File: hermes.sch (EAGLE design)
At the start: 29 parts, among them IC1 MIC5219-3.3BML

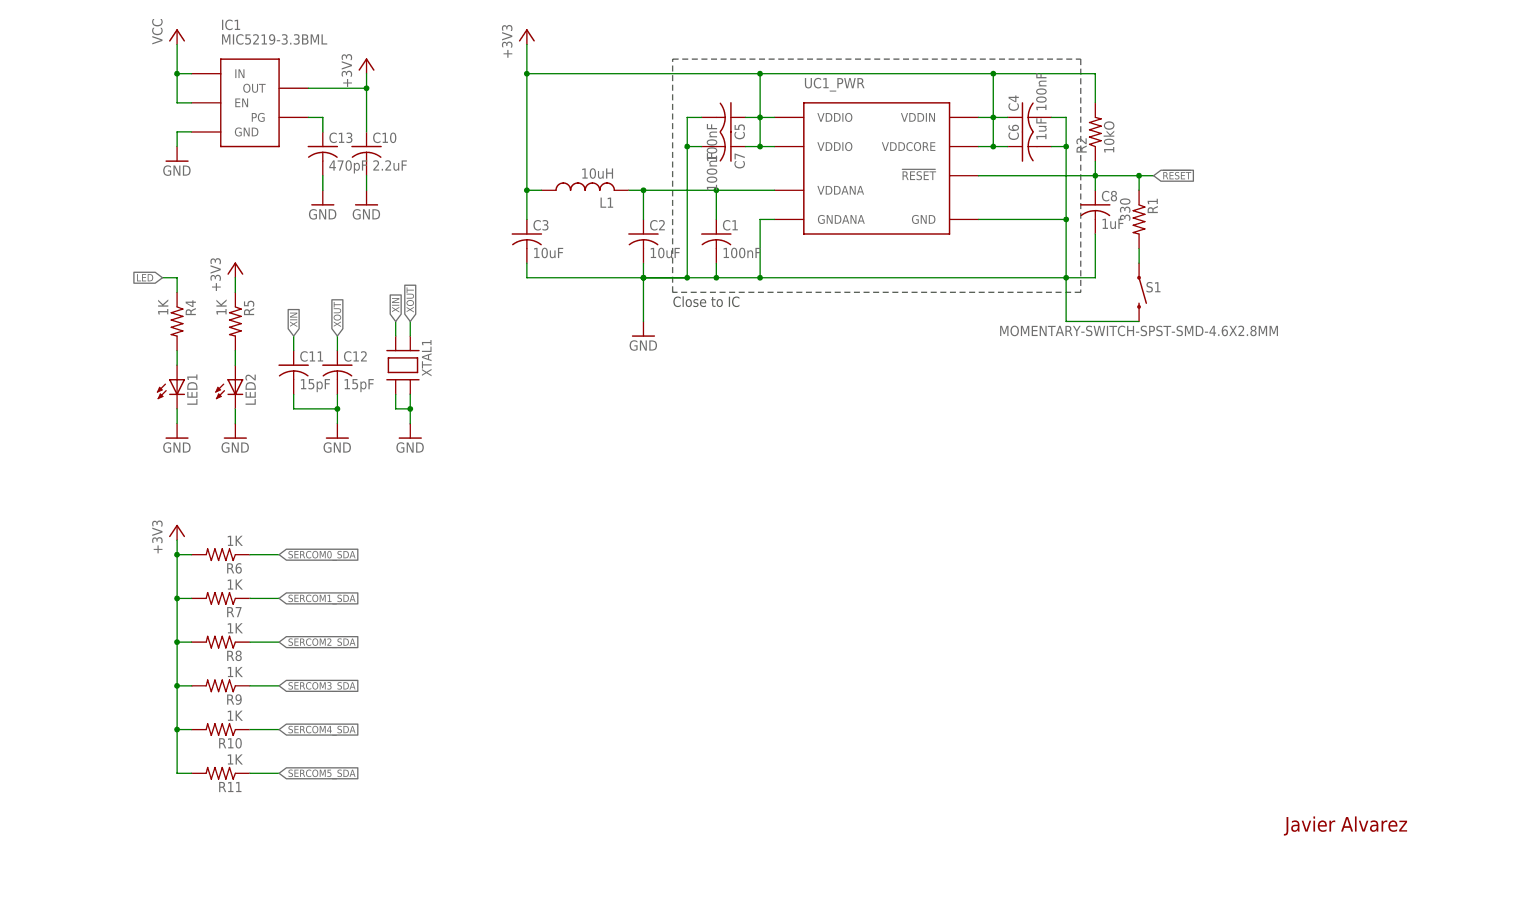
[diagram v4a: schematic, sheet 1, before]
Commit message: -Remove Reset switch -Add programming port -Correct minor connection issues
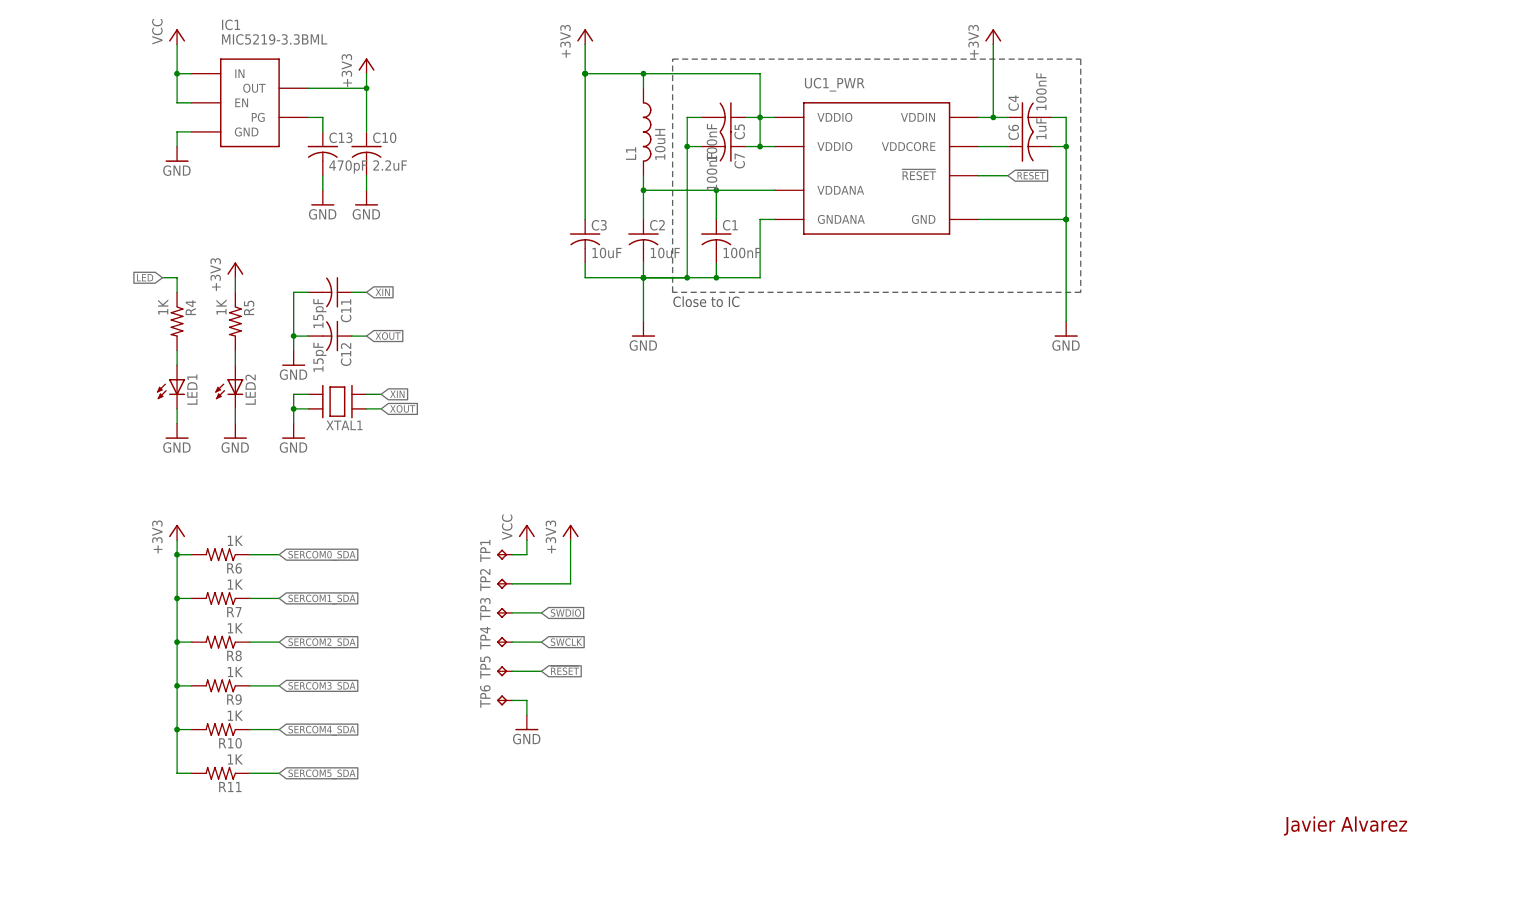
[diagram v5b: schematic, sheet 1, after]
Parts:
- removed C8: 1uF, rcl:C-USC0201
- removed R1: 330, rcl:R-US_R0201
- removed R2: 10kO, rcl:R-US_R0201
- removed S1: MOMENTARY-SWITCH-SPST-SMD-4.6X2.8MM, SparkFun-Switches:MOMENTARY-SWITCH-SPST-SMD-4.6X2.8MM
- added TP1, TP2, TP3, TP4, TP5, TP6: TPB2,54, testpad:TPB2,54
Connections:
- removed net N$5: R1.2, S1.1
- new net N$3: C6.1, UC1_PWR.VDDCORE
- net !RESET: now also TP5.TP; no longer C8.1, R1.1, R2.1
- net +3V3: now also TP2.TP; no longer C6.1, R2.2, UC1_PWR.VDDCORE
- net GND: now also TP6.TP; no longer C8.2, S1.2
- net SWCLK: now also TP4.TP
- net SWDIO: now also TP3.TP
- net VCC: now also TP1.TP
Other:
- moved on the sheet: C11, C12, C3, L1, XTAL1

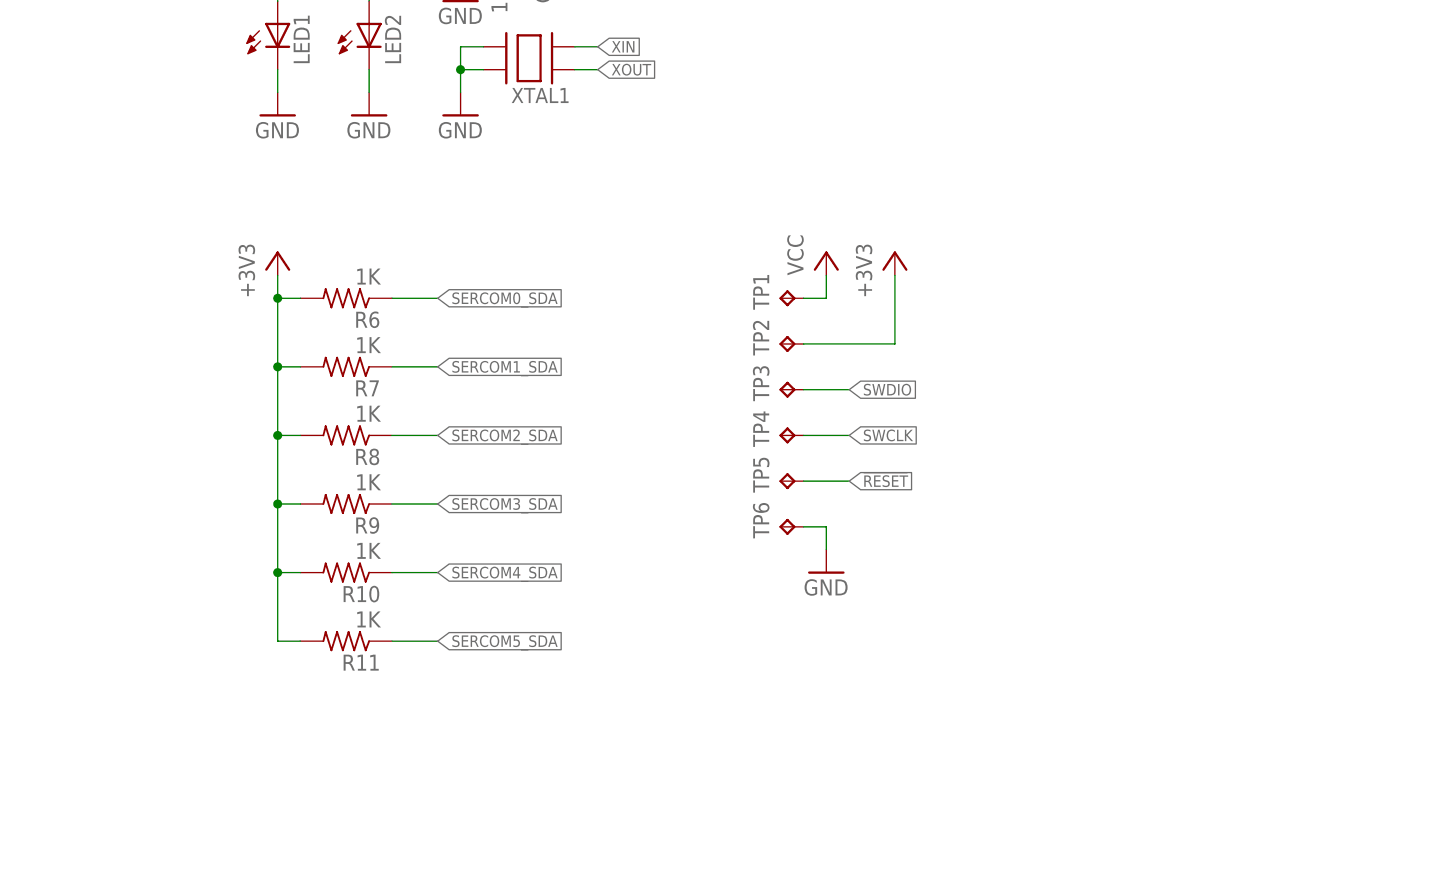
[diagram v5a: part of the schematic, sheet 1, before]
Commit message: -Correct README.md specifications -Add custom pads to library -Add programming connection to schematics
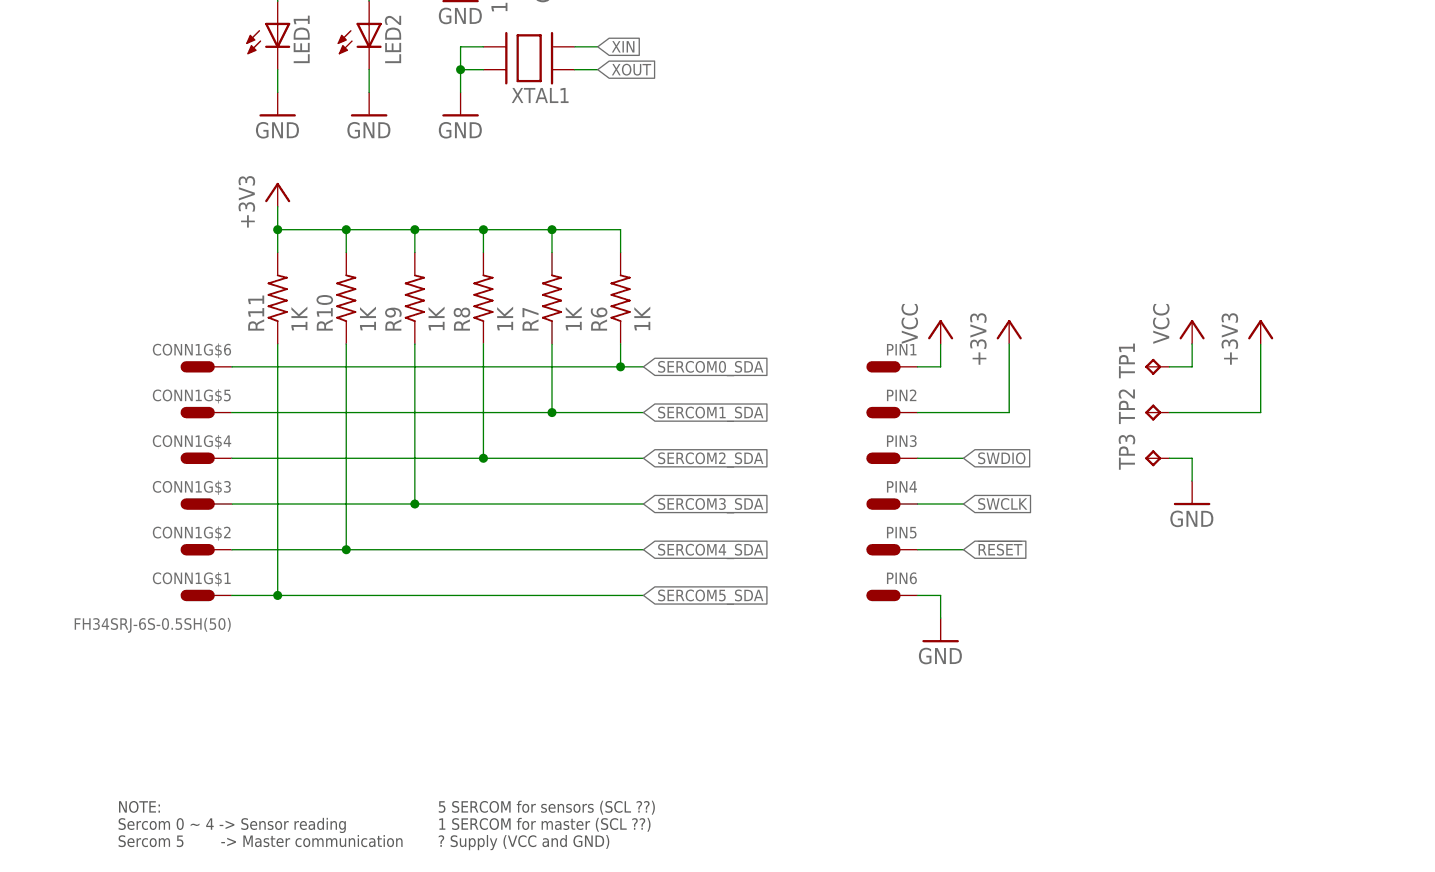
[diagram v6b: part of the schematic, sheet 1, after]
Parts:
- removed TP4, TP5, TP6: TPB2,54, testpad:TPB2,54
- added CONN1: FH34SRJ-6S-0.5SH(50), Hermes_lib:FH34SRJ-6S-0.5SH(50)
- added PIN1, PIN2, PIN3, PIN4, PIN5, PIN6: SINGLE-PIN, Hermes_lib:SINGLE-PIN
- TP1, TP2, TP3: value TPB2,54 -> TPB1,27; device testpad:TPB2,54 -> testpad:TPB1,27
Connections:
- net !RESET: now also PIN5.P$1; no longer TP5.TP
- net +3V3: now also PIN2.P$1
- net GND: now also PIN6.P$1, TP3.TP; no longer TP6.TP
- net SERCOM0_SDA: now also CONN1G$6.P$1
- net SERCOM1_SDA: now also CONN1G$5.P$1
- net SERCOM2_SDA: now also CONN1G$4.P$1
- net SERCOM3_SDA: now also CONN1G$3.P$1
- net SERCOM4_SDA: now also CONN1G$2.P$1
- net SERCOM5_SDA: now also CONN1G$1.P$1
- net SWCLK: now also PIN4.P$1; no longer TP4.TP
- net SWDIO: now also PIN3.P$1; no longer TP3.TP
- net VCC: now also PIN1.P$1
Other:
- note added: "5 SERCOM for sensors (SCL ??) 1 SERCOM for master (SCL ??) ? Supply (VCC and GND)"
- note added: "NOTE: Sercom 0 ~ 4 -> Sensor reading Sercom 5 -> Master communication"
- moved on the sheet: R10, R11, R6, R7, R8, R9, TP1, TP2, TP3

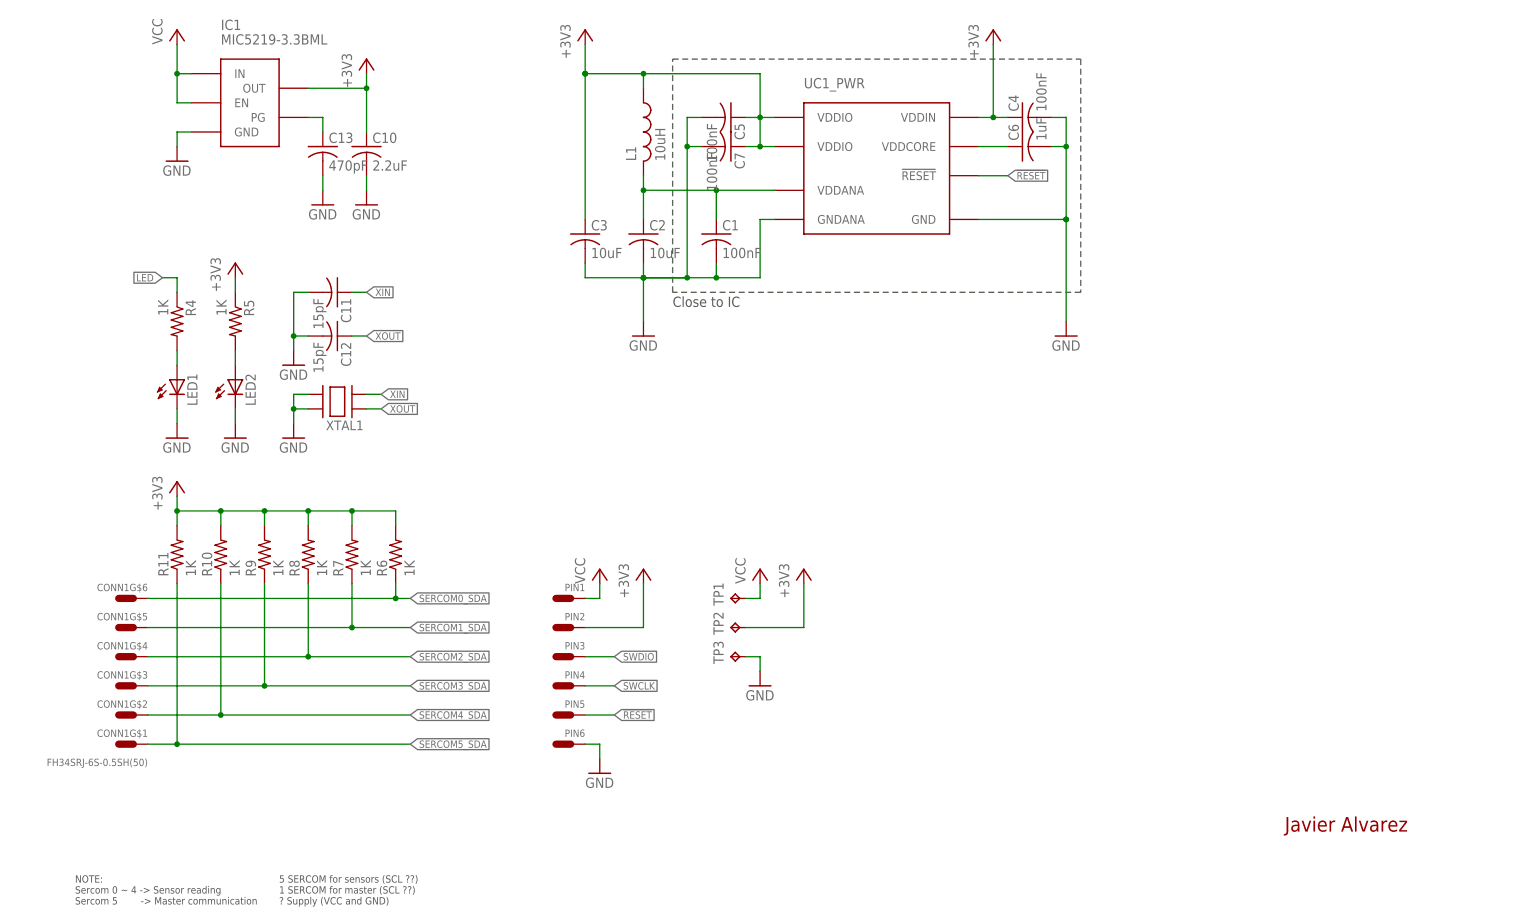
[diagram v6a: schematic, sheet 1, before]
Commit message: -Confirm cabling -Add information
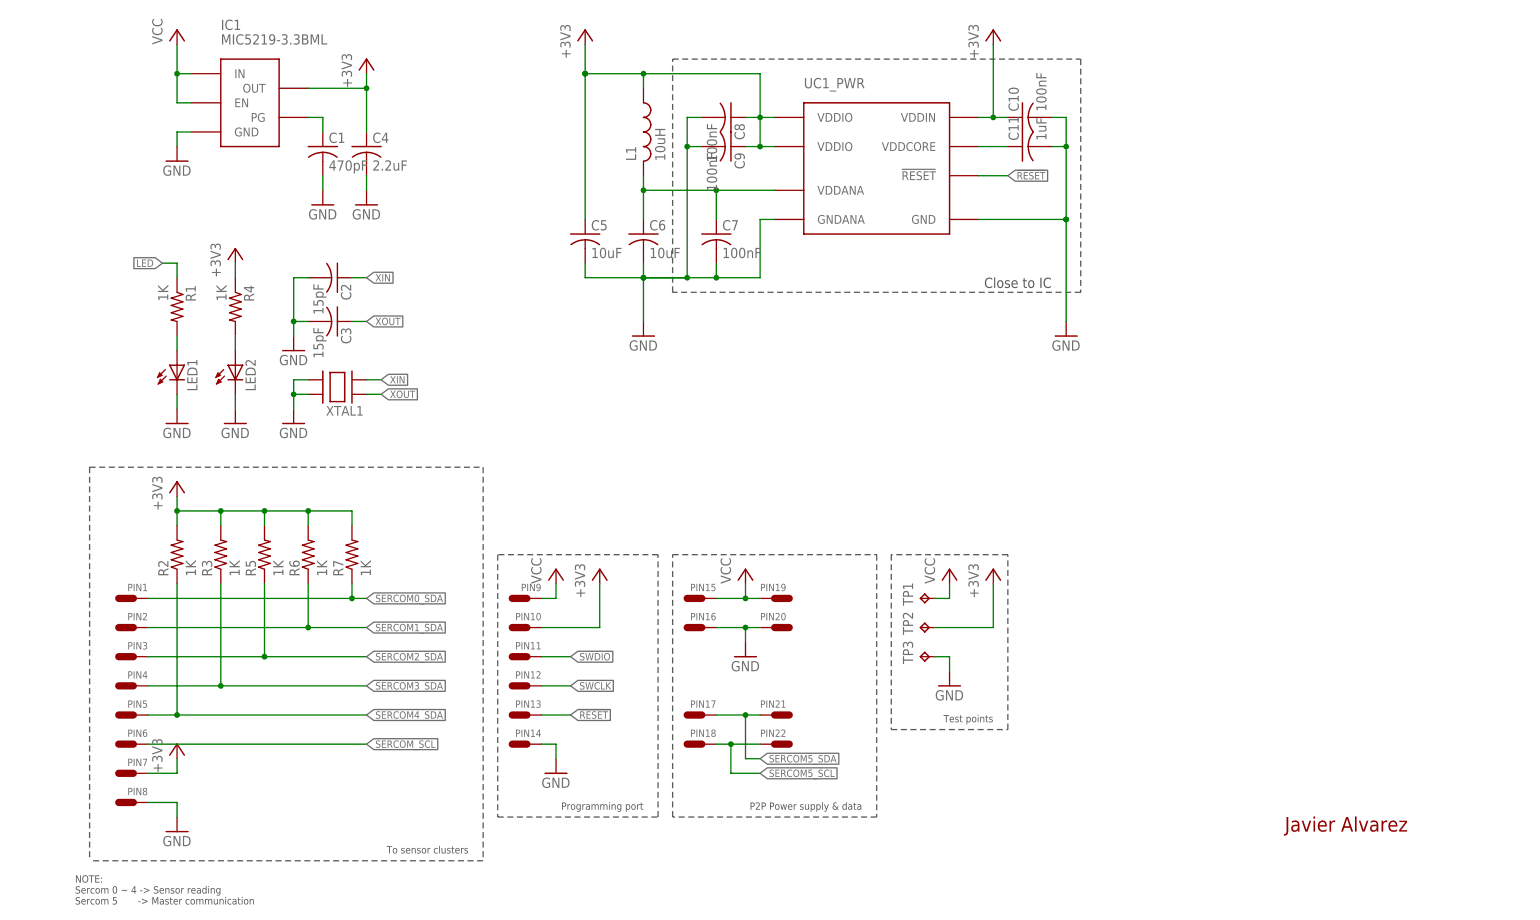
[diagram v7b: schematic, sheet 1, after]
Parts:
- removed C12: 15pF, rcl:C-USC0201
- removed C13: 470pF, rcl:C-USC0201
- removed CONN1: FH34SRJ-6S-0.5SH(50), Hermes_lib:FH34SRJ-6S-0.5SH(50)
- removed R8, R9: 1K, rcl:R-US_R0201
- added C8, C9: 100nF, rcl:C-USC0201
- added PIN10, PIN11, PIN12, PIN13, PIN14, PIN15, PIN16, PIN17, PIN18, PIN19, PIN20, PIN21, PIN22, PIN7, PIN8, PIN9: SINGLE-PIN, Hermes_lib:SINGLE-PIN
- added R1: 1K, rcl:R-US_R0201
- C1: value 100nF -> 470pF
- C10: value 2.2uF -> 100nF
- C11: value 15pF -> 1uF
- C2, C3: value 10uF -> 15pF
- C4: value 100nF -> 2.2uF
- C5: value 100nF -> 10uF
- C6: value 1uF -> 10uF
- renumbered R10 to R3, R11 to R2
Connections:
- removed net SERCOM0_SCL: UC1_IO.PA09
- removed net SERCOM1_SCL: UC1_IO.PA17
- removed net SERCOM2_SCL: UC1_IO.PA13
- removed net SERCOM3_SCL: UC1_IO.PA23
- removed net SERCOM4_SCL: UC1_IO.PB09
- new net SERCOM_SCL: PIN6.P$1, UC1_IO.PA09, UC1_IO.PA13, UC1_IO.PA17, UC1_IO.PA23, UC1_IO.PB09
- net !RESET: now also PIN13.P$1; no longer PIN5.P$1
- net +3V3: now also C8.1, C9.1, PIN10.P$1, PIN7.P$1, R4.1, R5.2; no longer C3.1, C7.1, PIN2.P$1, R5.1, R8.2, R9.2
- net GND: now also C8.2, C9.2, PIN14.P$1, PIN16.P$1, PIN20.P$1, PIN8.P$1; no longer C12.2, C13.2, PIN6.P$1
- net LED: now also R1.1; no longer R4.1
- net N$1: now also C6.1, C7.1; no longer C1.1, C2.1
- net N$2: now also C1.1; no longer C13.1
- net N$3: now also C11.1; no longer C6.1
- net N$6: now also R1.2; no longer R4.2
- net N$7: now also R4.2; no longer R5.2
- net SERCOM0_SDA: now also PIN1.P$1, R7.1; no longer CONN1G$6.P$1, R6.1
- net SERCOM1_SDA: now also PIN2.P$1, R6.1; no longer CONN1G$5.P$1, R7.1
- net SERCOM2_SDA: now also PIN3.P$1, R5.1; no longer CONN1G$4.P$1, R8.1
- net SERCOM3_SDA: now also PIN4.P$1, R3.1; no longer CONN1G$3.P$1, R9.1
- net SERCOM4_SDA: now also PIN5.P$1, R2.1; no longer CONN1G$2.P$1, R3.1
- net SERCOM5_SCL: now also PIN18.P$1, PIN22.P$1
- net SERCOM5_SDA: now also PIN17.P$1, PIN21.P$1; no longer CONN1G$1.P$1, R2.1
- net SWCLK: now also PIN12.P$1; no longer PIN4.P$1
- net SWDIO: now also PIN11.P$1; no longer PIN3.P$1
- net VCC: now also PIN15.P$1, PIN19.P$1, PIN9.P$1; no longer PIN1.P$1
- net XIN: now also C2.1; no longer C11.1
- net XOUT: now also C3.1; no longer C12.1
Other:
- note added: "P2P Power supply & data"
- note added: "Programming port"
- note added: "Test points"
- note added: "To sensor clusters"
- note removed: "5 SERCOM for sensors (SCL ??) 1 SERCOM for master (SCL ??) ? Supply (VCC and GND)"
- moved on the sheet: C1, C10, C11, C2, C3, C4, C5, C6, C7, LED1, LED2, PIN1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
